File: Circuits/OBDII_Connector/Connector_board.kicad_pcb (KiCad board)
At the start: 4 copper layers, 49.6 x 48.9 mm, 30 parts, among them J2 USB_C_Receptacle_USB2.0_14P, J4 Conn_02x08_Top_Bottom, J5 Conn_02x07_Counter_Clockwise, Q1 2N7002, Q2 MMDT3904, U1 TCAN3404, U2 ESP32-S3-WROOM-1, U3 AP2112K-3.3, U5 LM5164DDA, U7 CP2102N-Axx-xQFN24

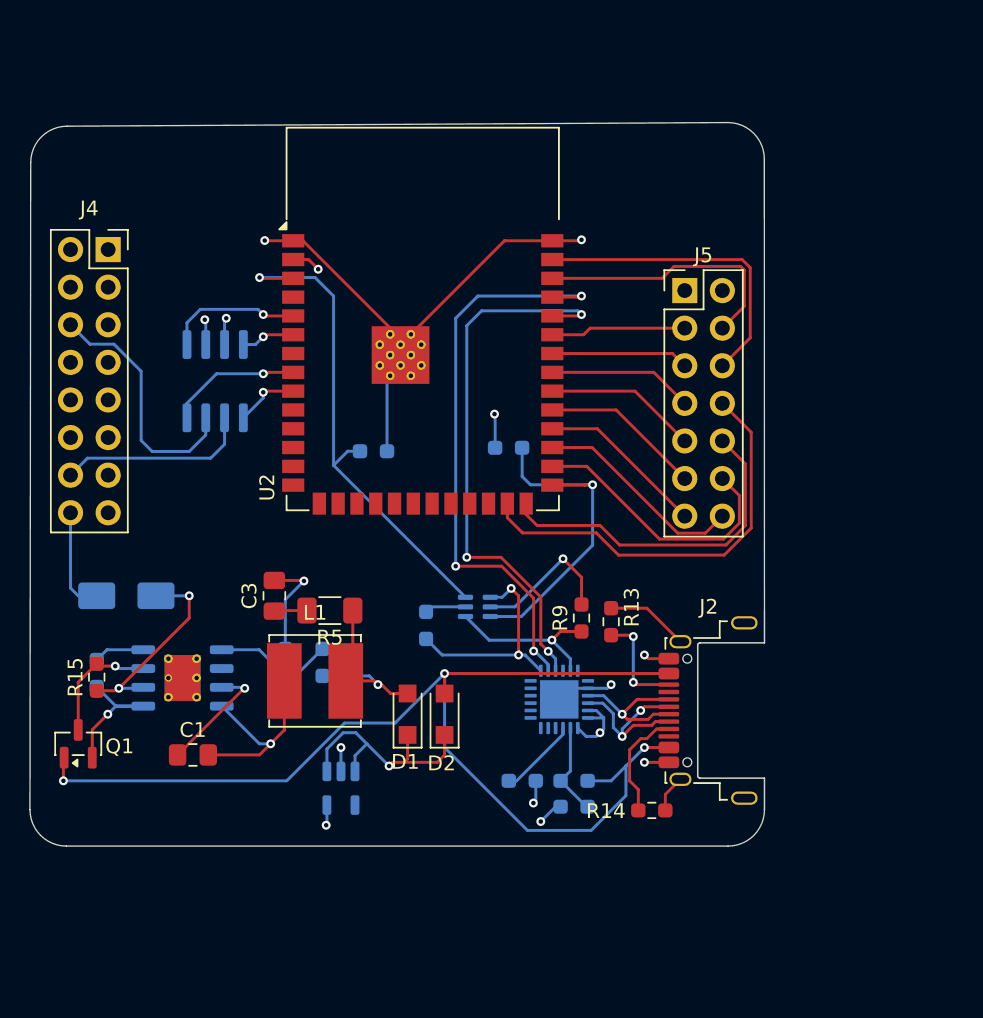
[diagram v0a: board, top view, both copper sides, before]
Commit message: Full redesign of connector board, including removal of USB flashing. This is now done by the flasher board.
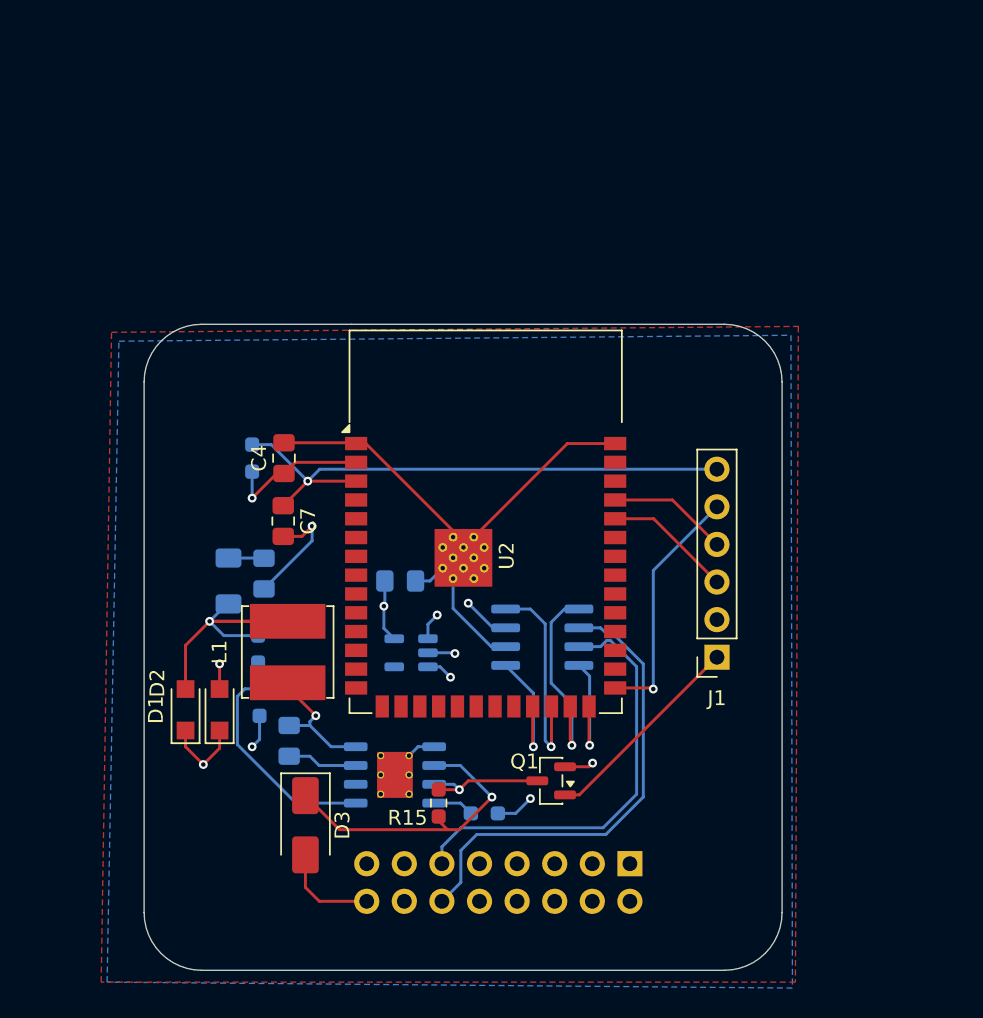
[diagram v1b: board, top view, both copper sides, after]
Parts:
- removed J4: Conn_02x08_Top_Bottom, Connector_PinSocket_2.54mm:PinSocket_2x08_P2.54mm_Vertical
- removed J5: Conn_02x07_Counter_Clockwise, Connector_PinHeader_2.54mm:PinHeader_2x07_P2.54mm_Vertical
- removed Q2: MMDT3904, Package_TO_SOT_SMD:SOT-363_SC-70-6
- removed R10, R8, R9: 1k, Resistor_SMD:R_0603_1608Metric_Pad0.98x0.95mm_HandSolder
- removed R11: 22k, Resistor_SMD:R_0603_1608Metric_Pad0.98x0.95mm_HandSolder
- removed R12: 47k, Resistor_SMD:R_0603_1608Metric_Pad0.98x0.95mm_HandSolder
- removed R13, R14: 5.1k, Resistor_SMD:R_0603_1608Metric_Pad0.98x0.95mm_HandSolder
- removed R17: 10k, Resistor_SMD:R_0603_1608Metric_Pad0.98x0.95mm_HandSolder
- removed U7: CP2102N-Axx-xQFN24, Package_DFN_QFN:QFN-24-1EP_4x4mm_P0.5mm_EP2.6x2.6mm
- added C4: 1uF, Capacitor_SMD:C_0805_2012Metric_Pad1.18x1.45mm_HandSolder, F.Cu at (80.7, 71.7)
- added C5: 4.7uF, Capacitor_SMD:C_0805_2012Metric_Pad1.18x1.45mm_HandSolder, B.Cu at (88.5, 80.0)
- added C7: 0.1uF, Capacitor_SMD:C_0805_2012Metric_Pad1.18x1.45mm_HandSolder, F.Cu at (80.6, 76.0)
- added J1: Conn_01x06_Pin, Connector_PinSocket_2.54mm:PinSocket_1x06_P2.54mm_Vertical, F.Cu at (109.9, 85.2)
- C1, C3, R5: moved to B.Cu
- D3: moved to F.Cu
- J2: value USB_C_Receptacle_USB2.0_14P -> Conn_02x08_Top_Bottom; footprint Connector_USB:USB_C_Receptacle_Amphenol_12401948E412A -> Connector_PinSocket_2.54mm:PinSocket_2x08_P2.54mm_Vertical; moved to B.Cu
- moved Q1 32.0 mm to (98.7, 93.5), turned to 180 degrees
- moved U1 28.1 mm to (98.1, 83.8), turned to 0 degrees
- moved R2 27.8 mm to (94.2, 95.7), turned to 0 degrees
- moved R15 24.6 mm to (91.1, 95.0)
- moved D3 19.7 mm to (82.1, 96.5), turned to -90 degrees
- moved R16 17.3 mm to (78.5, 71.7), turned to 90 degrees
- moved U5 15.8 mm to (88.1, 93.1), turned to 180 degrees
- moved D2 15.2 mm to (76.3, 88.7)
- moved D1 15.0 mm to (74.0, 88.7)
- moved U2 14.3 mm to (94.3, 76.0)
- moved J2 12.9 mm to (104.0, 99.1)
- moved U3 10.3 mm to (89.2, 84.8), turned to 180 degrees
- moved R5 7.14 mm to (76.9, 80.0), turned to 90 degrees
- moved C1 6.57 mm to (81.0, 90.8), turned to 90 degrees
- moved R3 4.44 mm to (78.9, 84.6), turned to -90 degrees
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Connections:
- R16 pad 1: /ESP_IO0 -> +3.3V
- R16 pad 2: GND -> /ESP_EN
- U1 pad 6: /CANL -> /CAN-
- U1 pad 7: /CANH -> /CAN+
- U2 pad 23: unconnected-(U2-IO21-Pad23) -> /CAN_TXD
- U2 pad 24: unconnected-(U2-IO47-Pad24) -> /CAN_RXD
- U2 pad 25: /LCD_LED -> /TCAN3404_SHDN
- U2 pad 26: /LCD_T_CLK -> /TCAN3404_STB
- U2 pad 28: /LCD_T_DIN -> unconnected-(U2-IO35-Pad28)
- U2 pad 29: /LCD_T_IRQ -> unconnected-(U2-IO36-Pad29)
- U2 pad 30: /LCD_T_DO -> unconnected-(U2-IO37-Pad30)
- U2 pad 31: /LCD_T_CS -> unconnected-(U2-IO38-Pad31)
- U2 pad 32: /LCD_MISO -> unconnected-(U2-IO39-Pad32)
- U2 pad 33: /LCD_SCK -> unconnected-(U2-IO40-Pad33)
- U2 pad 34: /LCD_DC -> unconnected-(U2-IO41-Pad34)
- U2 pad 35: /LCD_CS -> unconnected-(U2-IO42-Pad35)
- U2 pad 38: /LCD_RESET -> unconnected-(U2-IO2-Pad38)
- U2 pad 39: /LCD_MOSI -> unconnected-(U2-IO1-Pad39)
- U2 pad 5: /CAN_TXD -> unconnected-(U2-IO5-Pad5)
- U2 pad 6: /CAN_RXD -> unconnected-(U2-IO6-Pad6)
- U2 pad 8: /TCAN3404_STB -> unconnected-(U2-IO15-Pad8)
- U2 pad 9: /TCAN3404_SHDN -> unconnected-(U2-IO16-Pad9)
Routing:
- net /CAN-: track 0.00 -> 32.1 mm
- net /ESP_TX: track 39.4 -> 8.12 mm, vias 3 -> 0
- net /CAN+: track 0.00 -> 29.2 mm
- net /ESP_RX: track 37.4 -> 8.65 mm, vias 3 -> 0
- net /LCD_LED: track 28.5 -> 0.00 mm
- net /USB_VBUS: track 75.8 -> 49.6 mm, vias 3 -> 1
- net /LCD_T_CLK: track 23.3 -> 0.00 mm
- net /LCD_MOSI: track 21.0 -> 0.00 mm
- net /LCD_T_DIN: track 18.6 -> 0.00 mm
- net /LCD_RESET: track 17.9 -> 0.00 mm
- net /CANH: track 17.0 -> 0.00 mm
- net GND: track 70.3 -> 53.8 mm, vias 11 -> 5
- net /5v_SOURCE: track 16.7 -> 32.9 mm, vias 1 -> 3
- net /RTS: track 15.0 -> 0.00 mm, vias 2 -> 0
- net /LCD_T_IRQ: track 14.4 -> 0.00 mm
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- added copper zone on B.Cu, net GND
- added copper zone on F.Cu, net GND
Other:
- board size 49.6 x 48.9 mm -> 43.1 x 43.6 mm

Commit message: Updated portside schematic
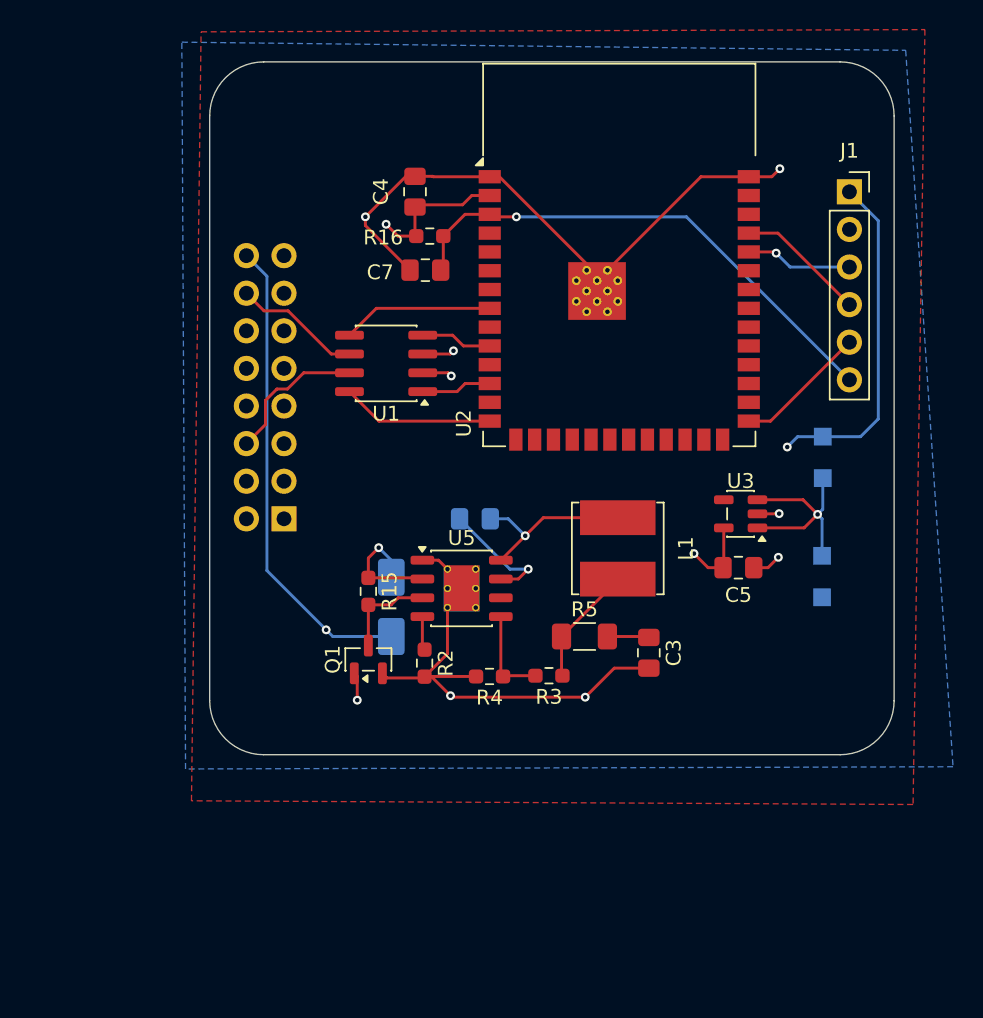
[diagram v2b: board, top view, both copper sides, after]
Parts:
- C3, C5, R16, R2, R3, R4, R5, U1, U3, U5: moved to F.Cu
- D1, D2, D3: moved to B.Cu
- moved D2 44.2 mm to (117.0, 71.7)
- moved D1 43.9 mm to (117.0, 79.7), turned to -90 degrees
- moved J2 33.0 mm to (80.7, 75.8), turned to 0 degrees
- moved J1 32.7 mm to (118.8, 53.7), turned to 0 degrees
- moved C3 26.5 mm to (105.3, 84.8)
- moved R5 24.3 mm to (101.0, 83.8), turned to 0 degrees
- moved U3 24.2 mm to (111.5, 75.5)
- moved L1 23.4 mm to (103.2, 77.8), turned to -90 degrees
- moved C5 22.9 mm to (111.3, 79.1)
- moved U1 21.3 mm to (87.5, 65.3), turned to 180 degrees
- moved U2 20.2 mm to (103.3, 58.0)
- moved C4 20.1 mm to (89.5, 53.7)
- moved R3 19.7 mm to (98.5, 86.4), turned to 180 degrees
- moved C1 19.6 mm to (93.5, 75.8), turned to 0 degrees
- moved C7 19.5 mm to (90.2, 59.0), turned to 180 degrees
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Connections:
- U2 pad 10: unconnected-(U2-IO17-Pad10) -> /CAN_RXD
- U2 pad 12: unconnected-(U2-IO8-Pad12) -> /CAN_TXD
- U2 pad 14: unconnected-(U2-USB_D+-Pad14) -> /TCAN3404_STB
- U2 pad 23: /CAN_TXD -> unconnected-(U2-IO21-Pad23)
- U2 pad 24: /CAN_RXD -> unconnected-(U2-IO47-Pad24)
- U2 pad 25: /TCAN3404_SHDN -> unconnected-(U2-IO48-Pad25)
- U2 pad 26: /TCAN3404_STB -> unconnected-(U2-IO45-Pad26)
- U2 pad 8: unconnected-(U2-IO15-Pad8) -> /TCAN3404_SHDN
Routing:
- net Net-(D3-A): track 6.73 -> 32.1 mm, vias 0 -> 1
- net /CAN-: track 32.1 -> 8.67 mm
- net GND: track 53.8 -> 74.0 mm, vias 5 -> 7
- net /CAN+: track 29.2 -> 9.90 mm
- net /5v_SOURCE: track 32.9 -> 14.4 mm, vias 3 -> 1
- net /5V_BUCK: track 21.2 -> 8.12 mm, vias 1 -> 0
- net /CAR_POS: track 20.4 -> 8.36 mm
- net /USB_VBUS: track 49.6 -> 61.4 mm, vias 1 -> 2
- net Net-(U5-FB): track 16.4 -> 6.32 mm
- net /CAN_RXD: track 14.3 -> 4.83 mm, vias 1 -> 0
- net /ESP_IO0: track 16.7 -> 9.01 mm, vias 1 -> 0
- net /CAN_TXD: track 9.02 -> 4.75 mm, vias 1 -> 0
- net /TCAN3404_SHDN: track 13.8 -> 10.2 mm, vias 1 -> 0
- net Net-(U5-BST): track 4.75 -> 8.17 mm, vias 0 -> 1
- net /ESP_EN: track 38.4 -> 35.0 mm
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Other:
- board size 43.1 x 43.6 mm -> 46.2 x 46.8 mm
